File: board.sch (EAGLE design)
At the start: 64 parts, among them K1 FTR-K1C, K2 FTR-K1C, K3 FTR-K1C, K4 FTR-K1C, X6 PN61729-S

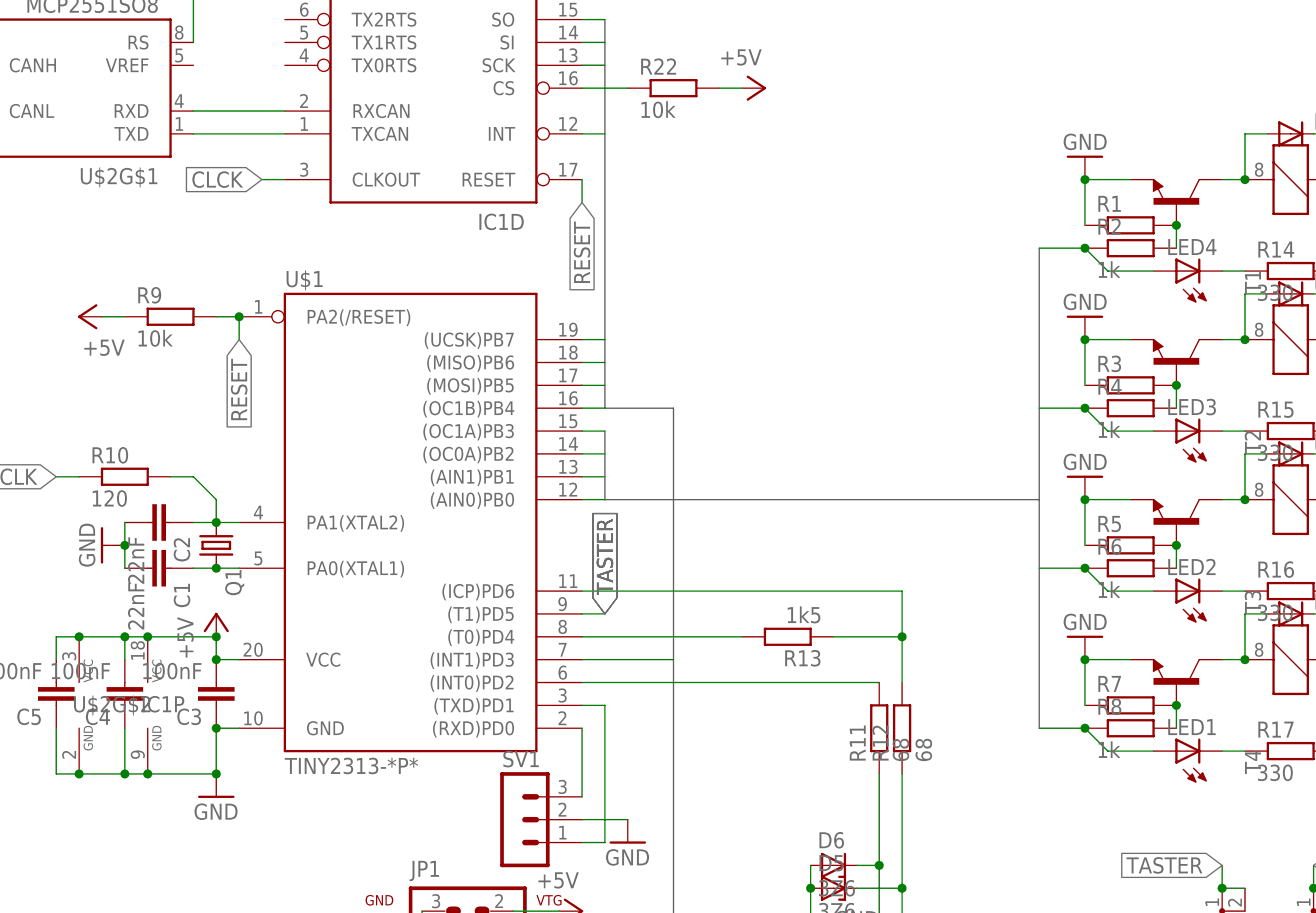
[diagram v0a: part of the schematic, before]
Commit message: polygon auf dem board angepasst, schaltplan angepasst
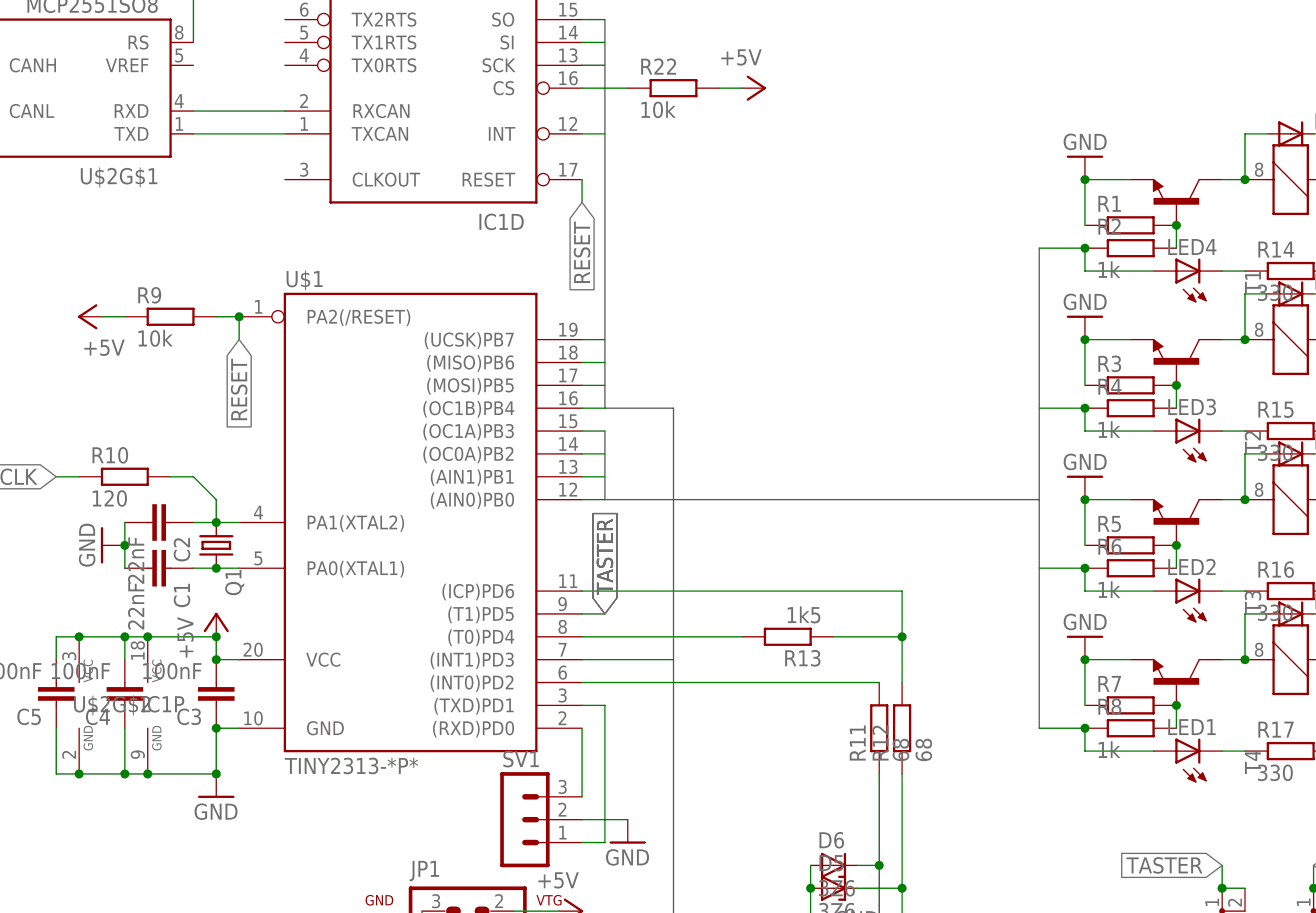
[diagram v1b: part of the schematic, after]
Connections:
- removed net CLCK: IC1D.CLKOUT
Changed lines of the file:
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@@
-</segment>
-</net>
-<net name="CLCK" class="0">
-<segment>
-<pinref part="IC1" gate="D" pin="CLKOUT"/>
-<wire x1="15.24" y1="111.76" x2="12.7" y2="111.76" width="0.1524" layer="91"/>
-<label x="12.7" y="111.76" size="1.778" layer="95" rot="R180" xref="yes"/>
 </segment>
 </net>
@@
 <wire x1="99.06" y1="50.8" x2="104.14" y2="50.8" width="0.1524" layer="91"/>
 <pinref part="LED1" gate="G$1" pin="A"/>
-<wire x1="104.14" y1="50.8" x2="106.68" y2="48.26" width="0.1524" layer="91"/>
-<wire x1="106.68" y1="48.26" x2="111.76" y2="48.26" width="0.1524" layer="91"/>
+<wire x1="104.14" y1="50.8" x2="104.14" y2="48.26" width="0.1524" layer="91"/>
+<wire x1="104.14" y1="48.26" x2="111.76" y2="48.26" width="0.1524" layer="91"/>
 <junction x="104.14" y="50.8"/>
 </segment>
@@
 <wire x1="99.06" y1="68.58" x2="104.14" y2="68.58" width="0.1524" layer="91"/>
 <pinref part="LED2" gate="G$1" pin="A"/>
-<wire x1="104.14" y1="68.58" x2="106.68" y2="66.04" width="0.1524" layer="91"/>
-<wire x1="106.68" y1="66.04" x2="111.76" y2="66.04" width="0.1524" layer="91"/>
+<wire x1="104.14" y1="68.58" x2="104.14" y2="66.04" width="0.1524" layer="91"/>
+<wire x1="104.14" y1="66.04" x2="111.76" y2="66.04" width="0.1524" layer="91"/>
 <junction x="104.14" y="68.58"/>
 </segment>
@@
 <wire x1="99.06" y1="86.36" x2="104.14" y2="86.36" width="0.1524" layer="91"/>
 <pinref part="LED3" gate="G$1" pin="A"/>
-<wire x1="104.14" y1="86.36" x2="106.68" y2="83.82" width="0.1524" layer="91"/>
-<wire x1="106.68" y1="83.82" x2="111.76" y2="83.82" width="0.1524" layer="91"/>
+<wire x1="104.14" y1="86.36" x2="104.14" y2="83.82" width="0.1524" layer="91"/>
+<wire x1="104.14" y1="83.82" x2="111.76" y2="83.82" width="0.1524" layer="91"/>
 <junction x="104.14" y="86.36"/>
 </segment>
@@
 <wire x1="99.06" y1="104.14" x2="104.14" y2="104.14" width="0.1524" layer="91"/>
 <pinref part="LED4" gate="G$1" pin="A"/>
-<wire x1="104.14" y1="104.14" x2="106.68" y2="101.6" width="0.1524" layer="91"/>
-<wire x1="106.68" y1="101.6" x2="111.76" y2="101.6" width="0.1524" layer="91"/>
+<wire x1="104.14" y1="104.14" x2="104.14" y2="101.6" width="0.1524" layer="91"/>
+<wire x1="104.14" y1="101.6" x2="111.76" y2="101.6" width="0.1524" layer="91"/>
 <junction x="104.14" y="104.14"/>
 </segment>
@@
 </sheet>
 </sheets>
+<errors>
+</errors>
 </schematic>
 </drawing>

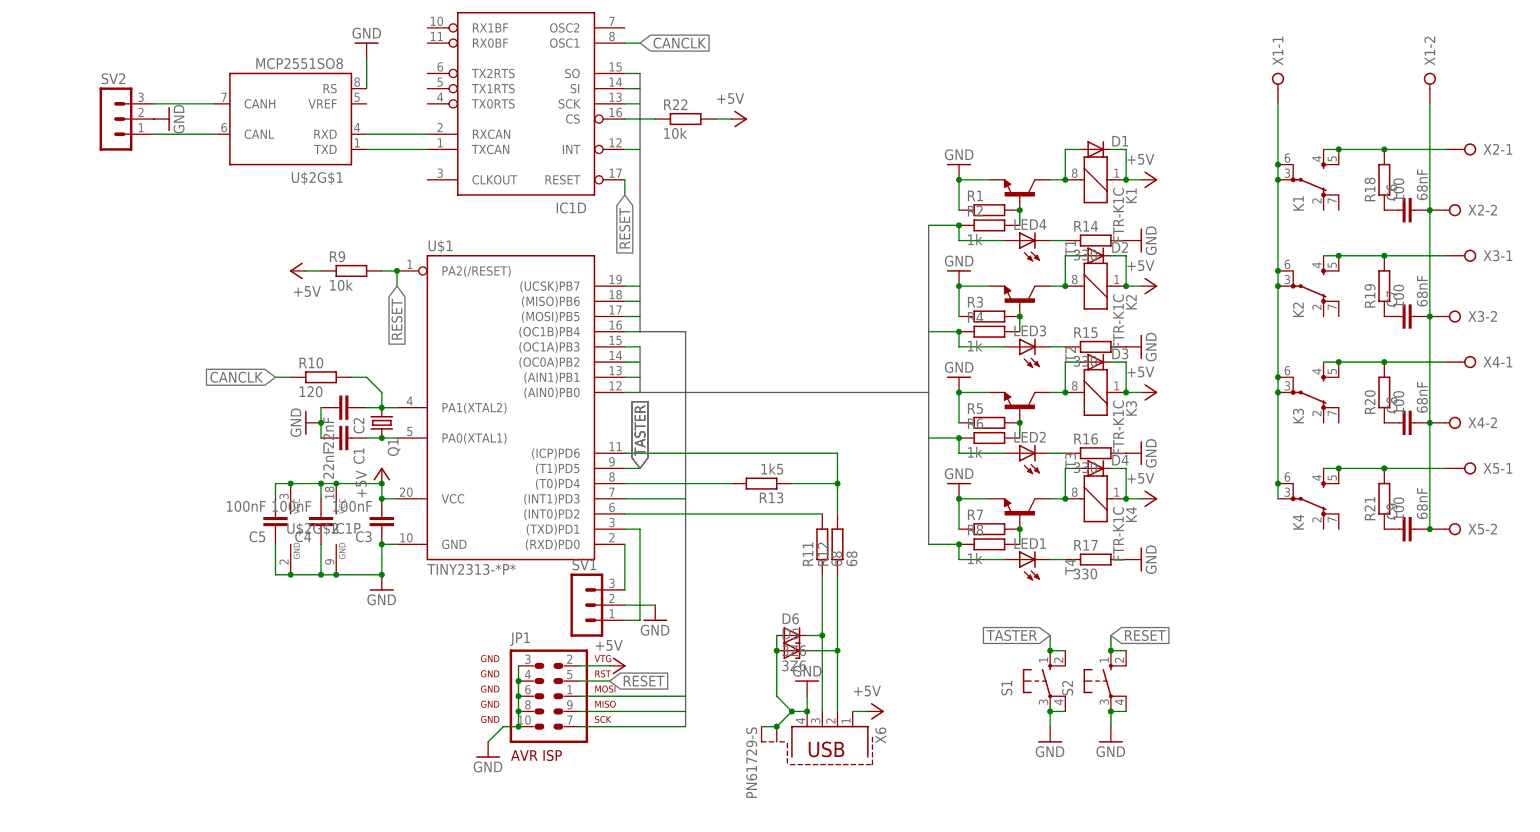
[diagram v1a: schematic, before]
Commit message: Adding choice of powersupply, enhancing supply of the tiny, board is a touch larger
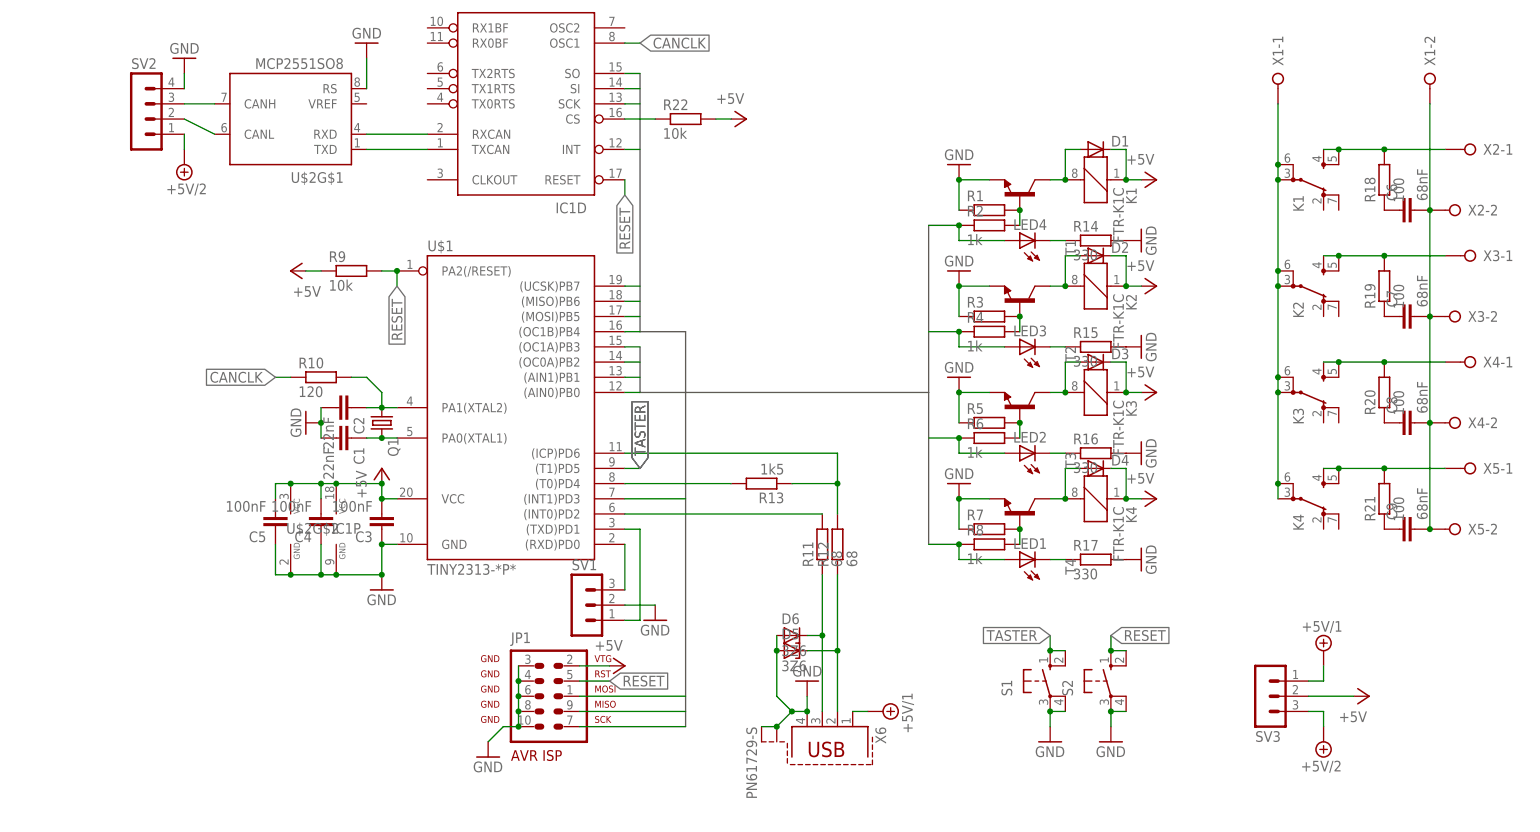
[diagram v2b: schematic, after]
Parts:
- added SV3: (no value), con-lstb:MA03-1
- SV2: device con-lstb:MA03-1 -> con-lstb:MA04-1; OC_FARNELL unknown -> (none); OC_NEWARK unknown -> (none)
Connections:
- new net +5V/1: SV3.1, X6.1
- new net +5V/2: SV2.1, SV3.3
- net +5V: now also SV3.2; no longer X6.1
- net GND: now also SV2.4; no longer SV2.2
- net N$35: now also SV2.2; no longer SV2.1
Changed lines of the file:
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@@
 <part name="R20" library="rcl" deviceset="R-EU_" device="0613/15" value="100"/>
 <part name="R21" library="rcl" deviceset="R-EU_" device="0613/15" value="100"/>
-<part name="SV2" library="con-lstb" deviceset="MA03-1" device="">
-<attribute name="MF" value=""/>
-<attribute name="MPN" value=""/>
-<attribute name="OC_FARNELL" value="unknown"/>
-<attribute name="OC_NEWARK" value="unknown"/>
-</part>
 <part name="GND17" library="supply1" deviceset="GND" device=""/>
 <part name="R22" library="rcl" deviceset="R-EU_" device="M0805" value="10k"/>
 <part name="P+9" library="supply1" deviceset="+5V" device=""/>
+<part name="SUPPLY1" library="supply2" deviceset="+5V/1" device=""/>
+<part name="SUPPLY2" library="supply2" deviceset="+5V/1" device=""/>
+<part name="SUPPLY3" library="supply2" deviceset="+5V/2" device=""/>
+<part name="SV3" library="con-lstb" deviceset="MA03-1" device=""/>
+<part name="SV2" library="con-lstb" deviceset="MA04-1" device=""/>
+<part name="SUPPLY4" library="supply2" deviceset="+5V/2" device=""/>
 </parts>
 <sheets>
@@
 <instance part="R10" gate="G$1" x="-2.54" y="78.74"/>
 <instance part="X6" gate="G$1" x="81.28" y="20.32" rot="R270"/>
-<instance part="P+8" gate="1" x="91.44" y="22.86" rot="R270"/>
+<instance part="P+8" gate="1" x="172.72" y="25.4" rot="MR90"/>
 <instance part="GND9" gate="1" x="78.74" y="27.94" rot="R180"/>
 <instance part="R11" gate="G$1" x="81.28" y="50.8" rot="R90"/>
@@
 <instance part="R20" gate="G$1" x="175.26" y="76.2" rot="R90"/>
 <instance part="R21" gate="G$1" x="175.26" y="58.42" rot="R90"/>
-<instance part="SV2" gate="G$1" x="-38.1" y="121.92"/>
-<instance part="GND17" gate="1" x="-27.94" y="121.92" rot="R90"/>
+<instance part="GND17" gate="1" x="-25.4" y="132.08" rot="R180"/>
 <instance part="R22" gate="G$1" x="58.42" y="121.92"/>
 <instance part="P+9" gate="1" x="68.58" y="121.92" rot="R270"/>
+<instance part="SUPPLY1" gate="G$1" x="91.44" y="22.86" rot="R270"/>
+<instance part="SUPPLY2" gate="G$1" x="165.1" y="33.02" rot="MR0"/>
+<instance part="SUPPLY3" gate="G$1" x="165.1" y="17.78" rot="MR180"/>
+<instance part="SV3" gate="G$1" x="154.94" y="25.4" rot="MR180"/>
+<instance part="SV2" gate="1" x="-33.02" y="124.46"/>
+<instance part="SUPPLY4" gate="G$1" x="-25.4" y="114.3" rot="R180"/>
 </instances>
 <busses>
@@
 </segment>
 <segment>
-<pinref part="X6" gate="G$1" pin="1"/>
-<pinref part="P+8" gate="1" pin="+5V"/>
-<wire x1="86.36" y1="22.86" x2="88.9" y2="22.86" width="0.1524" layer="91"/>
-</segment>
-<segment>
 <pinref part="R22" gate="G$1" pin="2"/>
 <pinref part="P+9" gate="1" pin="+5V"/>
 <wire x1="66.04" y1="121.92" x2="63.5" y2="121.92" width="0.1524" layer="91"/>
+</segment>
+<segment>
+<pinref part="P+8" gate="1" pin="+5V"/>
+<pinref part="SV3" gate="G$1" pin="2"/>
+<wire x1="162.56" y1="25.4" x2="170.18" y2="25.4" width="0.1524" layer="91"/>
 </segment>
 </net>
@@
 </segment>
 <segment>
-<pinref part="SV2" gate="G$1" pin="2"/>
+<pinref part="SV2" gate="1" pin="4"/>
 <pinref part="GND17" gate="1" pin="GND"/>
+<wire x1="-25.4" y1="129.54" x2="-25.4" y2="127" width="0.1524" layer="91"/>
 </segment>
 </net>
@@
 <segment>
 <pinref part="U$2" gate="G$1" pin="CANH"/>
-<pinref part="SV2" gate="G$1" pin="3"/>
-<wire x1="-20.32" y1="124.46" x2="-30.48" y2="124.46" width="0.1524" layer="91"/>
+<wire x1="-20.32" y1="124.46" x2="-25.4" y2="124.46" width="0.1524" layer="91"/>
+<pinref part="SV2" gate="1" pin="3"/>
 </segment>
 </net>
@@
 <segment>
 <pinref part="U$2" gate="G$1" pin="CANL"/>
-<pinref part="SV2" gate="G$1" pin="1"/>
-<wire x1="-20.32" y1="119.38" x2="-30.48" y2="119.38" width="0.1524" layer="91"/>
+<wire x1="-20.32" y1="119.38" x2="-25.4" y2="121.92" width="0.1524" layer="91"/>
+<pinref part="SV2" gate="1" pin="2"/>
 </segment>
 </net>
@@
 </segment>
 </net>
+<net name="+5V/1" class="0">
+<segment>
+<pinref part="X6" gate="G$1" pin="1"/>
+<pinref part="SUPPLY1" gate="G$1" pin="+5V/1"/>
+<wire x1="88.9" y1="22.86" x2="86.36" y2="22.86" width="0.1524" layer="91"/>
+</segment>
+<segment>
+<pinref part="SUPPLY2" gate="G$1" pin="+5V/1"/>
+<pinref part="SV3" gate="G$1" pin="1"/>
+<wire x1="165.1" y1="30.48" x2="165.1" y2="27.94" width="0.1524" layer="91"/>
+<wire x1="165.1" y1="27.94" x2="162.56" y2="27.94" width="0.1524" layer="91"/>
+</segment>
+</net>
+<net name="+5V/2" class="0">
+<segment>
+<pinref part="SUPPLY3" gate="G$1" pin="+5V/2"/>
+<pinref part="SV3" gate="G$1" pin="3"/>
+<wire x1="165.1" y1="20.32" x2="165.1" y2="22.86" width="0.1524" layer="91"/>
+<wire x1="165.1" y1="22.86" x2="162.56" y2="22.86" width="0.1524" layer="91"/>
+</segment>
+<segment>
+<pinref part="SV2" gate="1" pin="1"/>
+<pinref part="SUPPLY4" gate="G$1" pin="+5V/2"/>
+<wire x1="-25.4" y1="116.84" x2="-25.4" y2="119.38" width="0.1524" layer="91"/>
+</segment>
+</net>
